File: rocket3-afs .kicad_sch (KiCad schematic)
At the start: 113 parts, among them IC1 ISLA85005A, J1 POWER, J2 ARMING_PLUG, J3 SMA, J4 E-MATCH_DROGUE, J5 SWD, J6 E-MATCH_RECOVERY, M1 MG90S, M2 MG90S, M3 MG90S, M4 MG90s, Q1 Q_NMOS_GSD, Q2 Q_NMOS_GSD, Q3 BC547, Q4 Q_NMOS_GSD, Q5 Q_NMOS_GSD, U10 STM32G474RET6, U11 TPS25921AD, U5 MP1584EN-LF-Z, U8 MMC5983MA, U9 USBLC6-2SC6, Y1 16MHz

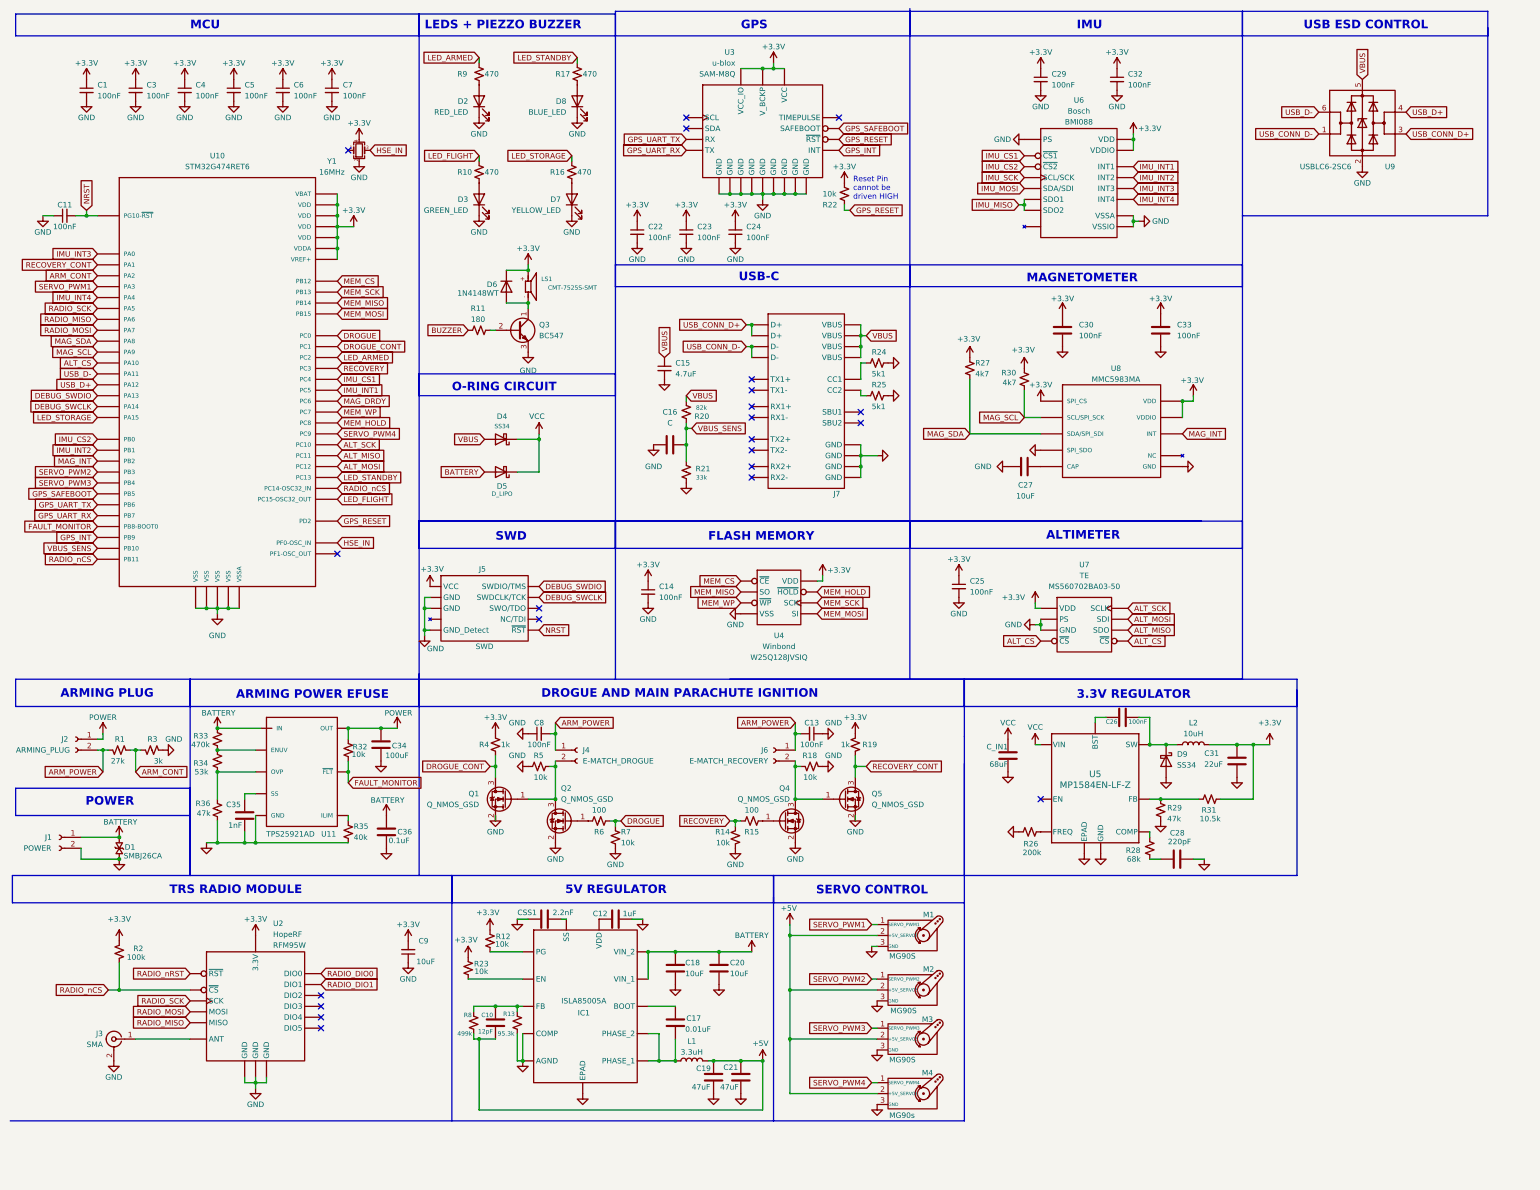
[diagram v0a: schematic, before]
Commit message: AFS 3.0 post PDR Edits, new MCU
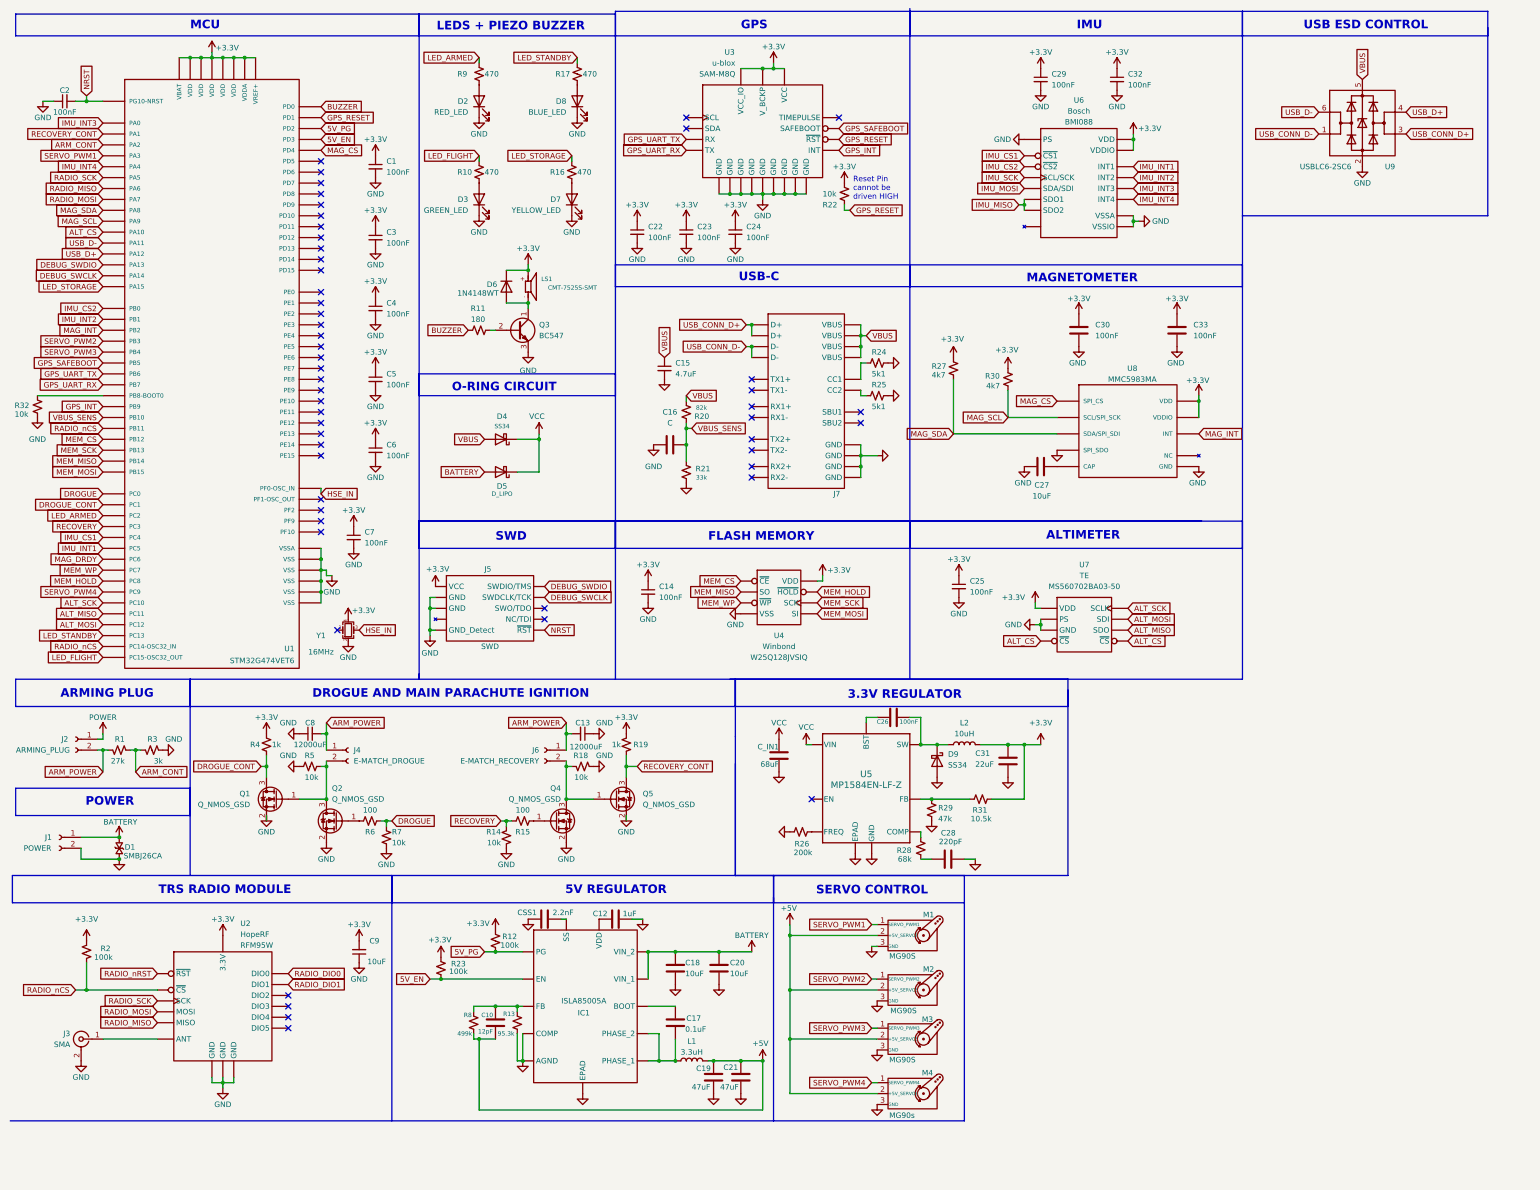
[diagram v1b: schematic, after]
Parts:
- removed C11: 100nF, Capacitor_SMD:C_0603_1608Metric, symbol Device:C_Small
- removed C34: 100uF, symbol Device:C
- removed C35: 1nF, symbol Device:C
- removed C36: 0.1uF, symbol Device:C
- removed R33: 470k, symbol Device:R_Small_US
- removed R34: 53k, symbol Device:R_Small_US
- removed R35: 40k, symbol Device:R_Small_US
- removed R36: 47k, symbol Device:R_Small_US
- removed U10: STM32G474RET6, STM32G474RET6:QFP50P1200X1200X160-64N, symbol STM32G474RET6:STM32G474RET6
- removed U11: TPS25921AD, TPS25921AD:SOIC127P599X175-8N, symbol TPS25921AD:TPS25921AD
- added C2: 100nF, Capacitor_SMD:C_0603_1608Metric, symbol Device:C_Small
- added U1: STM32G474VET6, STM32G474VET6:QFP50P1600X1600X160-100N, symbol STM32G474VET6:STM32G474VET6
- C13, C8: value 100nF -> 12000uF
- C17: value 0.01uF -> 0.1uF
- R12, R23: value 10k -> 100k
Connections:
- net FAULT_MONITOR is gone; now on net GND: R32.2
- net +3.3V: now also U1. (VSS)
- net ALT_CS: now also U1. (VSS)
- net ALT_MISO: now also U1. (VSS)
- net ALT_MOSI: now also U1. (VSS)
- net ALT_SCK: now also U1. (VSS)
- net ARM_CONT: now also U1. (VSS)
- net BUZZER: now also U1. (VSS)
- net DEBUG_SWCLK: now also U1. (VSS)
- net DEBUG_SWDIO: now also U1. (VSS)
- net DROGUE: now also U1. (VSS)
- net DROGUE_CONT: now also U1. (VSS)
- net GND: now also C2.1, U1. (VSS)
- net GPS_INT: now also U1. (VSS)
- net GPS_RESET: now also U1. (VSS)
- net GPS_SAFEBOOT: now also U1. (VSS)
- net GPS_UART_RX: now also U1. (VSS)
- net GPS_UART_TX: now also U1. (VSS)
- net HSE_IN: now also U1. (VSS)
- net IMU_CS1: now also U1. (VSS)
- net IMU_CS2: now also U1. (VSS)
- net IMU_INT1: now also U1. (VSS)
- net IMU_INT2: now also U1. (VSS)
- net IMU_INT3: now also U1. (VSS)
- net IMU_INT4: now also U1. (VSS)
- net LED_ARMED: now also U1. (VSS)
- net LED_FLIGHT: now also U1. (VSS)
- net LED_STANDBY: now also U1. (VSS)
- net LED_STORAGE: now also U1. (VSS)
- net MAG_DRDY: now also U1. (VSS)
- net MAG_INT: now also U1. (VSS)
- net MAG_SCL: now also U1. (VSS)
- net MAG_SDA: now also U1. (VSS)
- net MEM_CS: now also U1. (VSS)
- net MEM_HOLD: now also U1. (VSS)
- net MEM_MISO: now also U1. (VSS)
- net MEM_MOSI: now also U1. (VSS)
- net MEM_SCK: now also U1. (VSS)
- net MEM_WP: now also U1. (VSS)
- net NRST: now also C2.2, U1. (VSS)
- net POWER: no longer R32.1
- net RADIO_MISO: now also U1. (VSS)
- net RADIO_MOSI: now also U1. (VSS)
- net RADIO_SCK: now also U1. (VSS)
- net RADIO_nCS: now also U1. (VSS)
- net RECOVERY: now also U1. (VSS)
- net RECOVERY_CONT: now also U1. (VSS)
- net SERVO_PWM1: now also U1. (VSS)
- net SERVO_PWM2: now also U1. (VSS)
- net SERVO_PWM3: now also U1. (VSS)
- net SERVO_PWM4: now also U1. (VSS)
- net USB_D+: now also U1. (VSS)
- net USB_D-: now also U1. (VSS)
- net VBUS_SENS: now also U1. (VSS)
- net 5V_EN: now reaches IC1. (PHASE_1), R23.1
- net 5V_EN: now also U1. (VSS)
- net 5V_PG: now reaches IC1. (PHASE_1), R12.1
- net 5V_PG: now also U1. (VSS)
- new net: R32.1, U1. (VSS)
- new net MAG_CS: U1. (VSS), U8. (SCL/SPI_SCK)
- no-connect marks 22 -> 52
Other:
- note added: "LEDS + PIEZO BUZZER"
- note removed: "ARMING POWER EFUSE"
- note removed: "LEDS + PIEZZO BUZZER"
- moved on the sheet: C1, C13, C26, C27, C28, C3, C30, C31, C33, C4, C5, C6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

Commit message: Added two extra ematchesas backups, GSP Reset pin added external pull up resistor
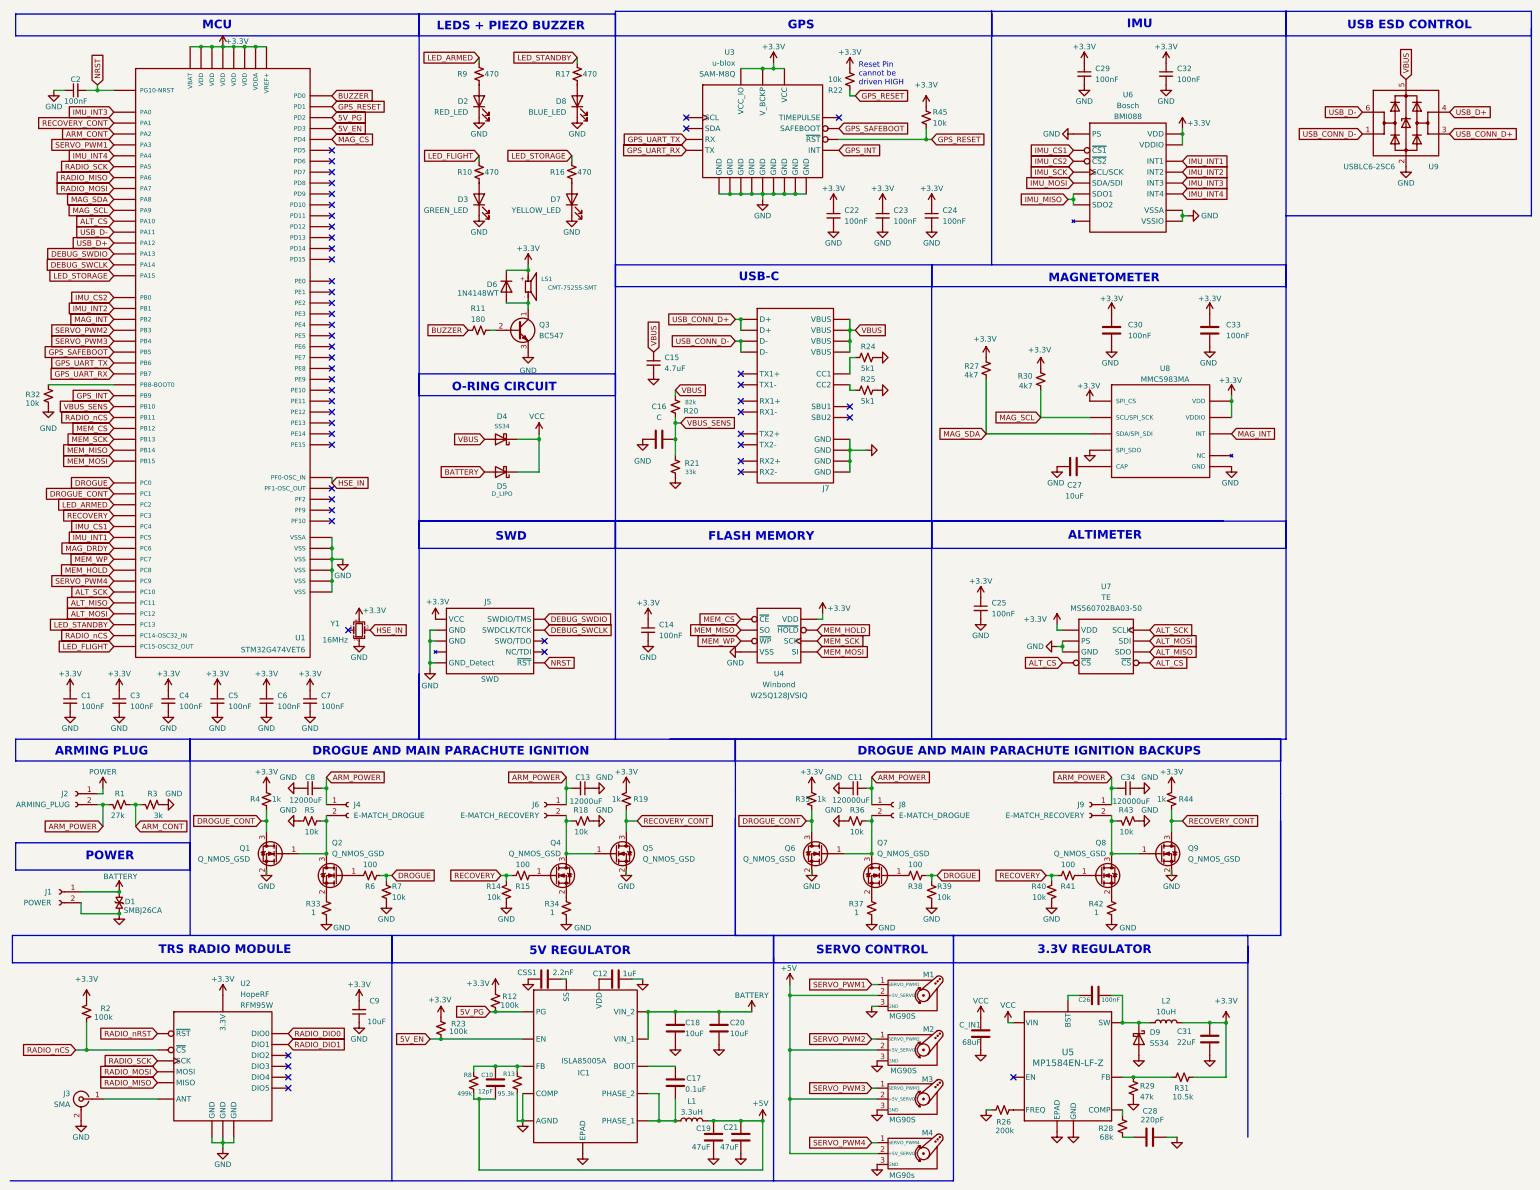
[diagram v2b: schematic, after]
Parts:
- added C11, C34: 120000uF, Capacitor_SMD:C_0603_1608Metric, symbol Device:C_Small
- added J8: E-MATCH_DROGUE, TerminalBlock:TerminalBlock_bornier-2_P5.08mm, symbol Connector:Conn_01x02_Socket
- added J9: E-MATCH_RECOVERY, TerminalBlock:TerminalBlock_bornier-2_P5.08mm, symbol Connector:Conn_01x02_Socket
- added Q6, Q7, Q8, Q9: Q_NMOS_GSD, Package_TO_SOT_SMD:TSOT-23, symbol Device:Q_NMOS_GSD
- added R33, R34, R37, R42: 1, symbol Device:R_Small_US
- added R35, R44: 1k, Resistor_SMD:R_0603_1608Metric, symbol Device:R_Small_US
- added R36, R39, R40, R43: 10k, Resistor_SMD:R_0603_1608Metric, symbol Device:R_Small_US
- added R38, R41: 100, Resistor_SMD:R_0603_1608Metric, symbol Device:R_Small_US
- added R45: 10k, symbol Device:R_Small_US
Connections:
- net +3.3V: now also R35.1, R44.1, R45.1
- net ARM_POWER: now also C11.2, C34.2, J8.1 (Pin_1), J9.1 (Pin_1)
- net DROGUE: now also R38.2, R39.1
- net DROGUE_CONT: now also Q6.3 (D), R35.2
- net GND: now also C11.1, C34.1, Q6.2 (S), Q9.2 (S), R33.2, R34.2, R36.2, R37.2, R39.2, R40.2, R42.2, R43.2; no longer Q2.2 (S), Q4.2 (S)
- net GPS_RESET: now also R45.2
- net MAG_CS: no longer U8. (SCL/SPI_SCK)
- net RECOVERY: now also R40.1, R41.1
- net RECOVERY_CONT: now also Q9.3 (D), R44.2
- new net: Q4.2 (S), R34.1
- new net: Q2.2 (S), R33.1
- new net: J8.2 (Pin_2), Q6.1 (G), Q7.3 (D), R36.1
- new net: Q7.1 (G), R38.1
- new net: J9.2 (Pin_2), Q8.3 (D), Q9.1 (G), R43.1
- new net: Q7.2 (S), R37.1
- new net: Q8.1 (G), R41.2
- new net: Q8.2 (S), R42.1
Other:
- note added: "DROGUE AND MAIN PARACHUTE IGNITION BACKUPS"
- moved on the sheet: C1, C10, C12, C13, C14, C15, C16, C17, C18, C19, C2, C20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
